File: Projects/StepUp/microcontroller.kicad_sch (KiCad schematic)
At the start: 31 parts, among them J1 USB_C_Receptacle_USB2.0_16P, J2 Conn_01x02, J3 Conn_02x03_Counter_Clockwise, SW1 SW_Push, SW2 SW_Push, U1 USBLC6-2SC6, U2 W25Q128JVS, U3 RP2040, Y1 ABM8-272-T3

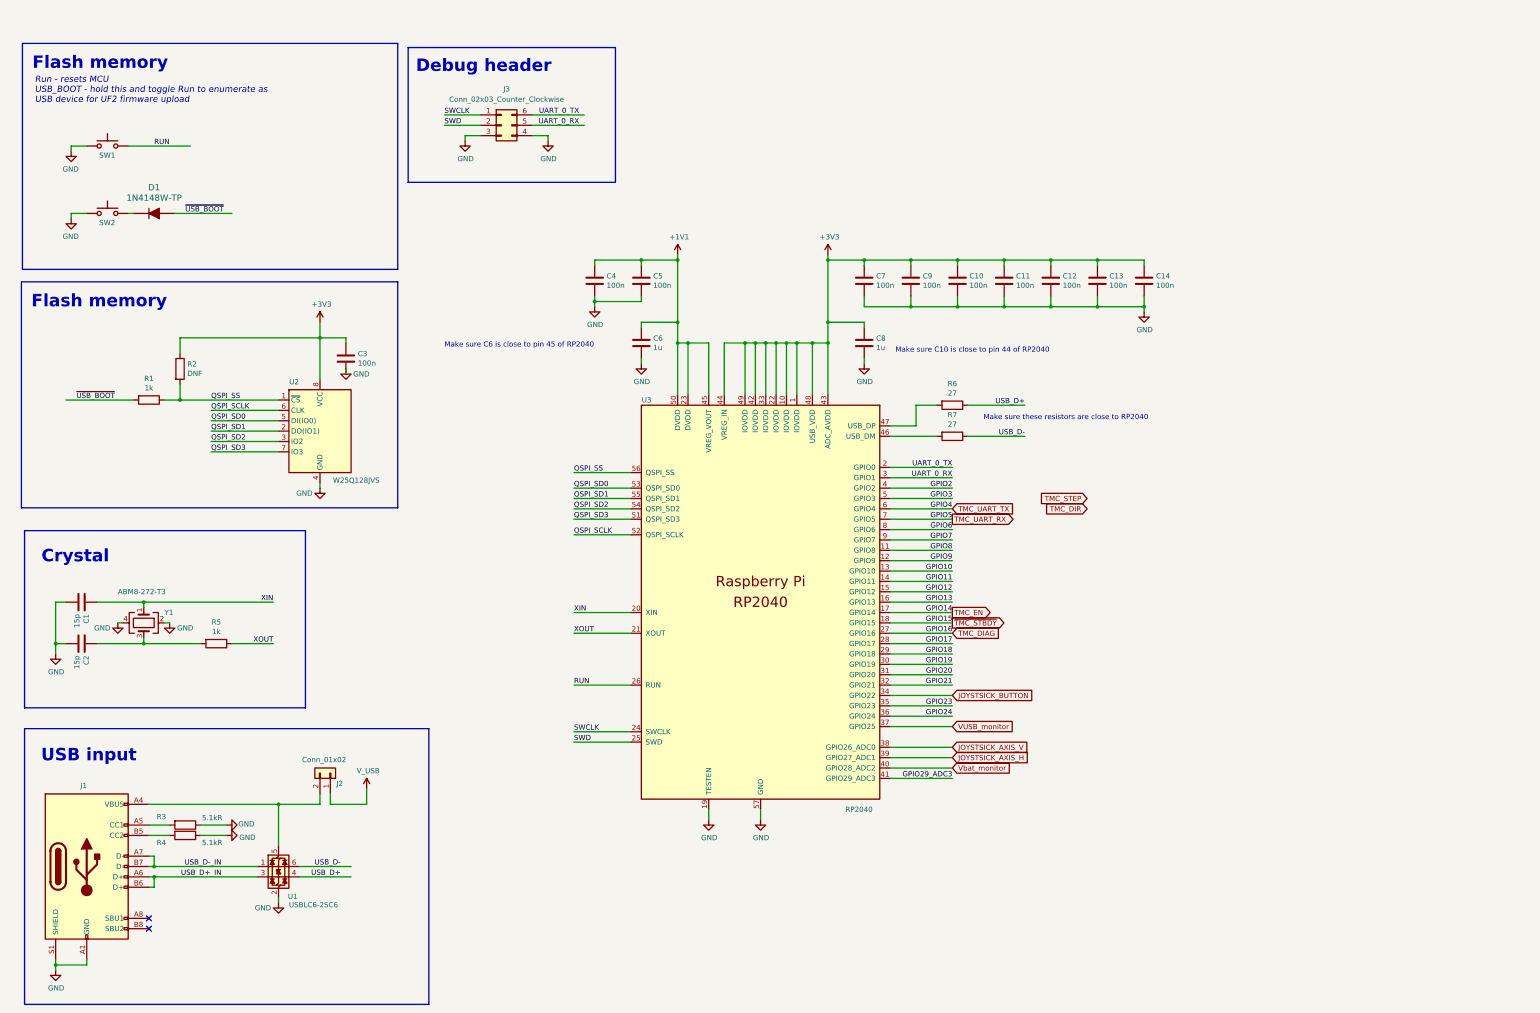
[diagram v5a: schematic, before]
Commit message: feat(schematic): Ready for layout
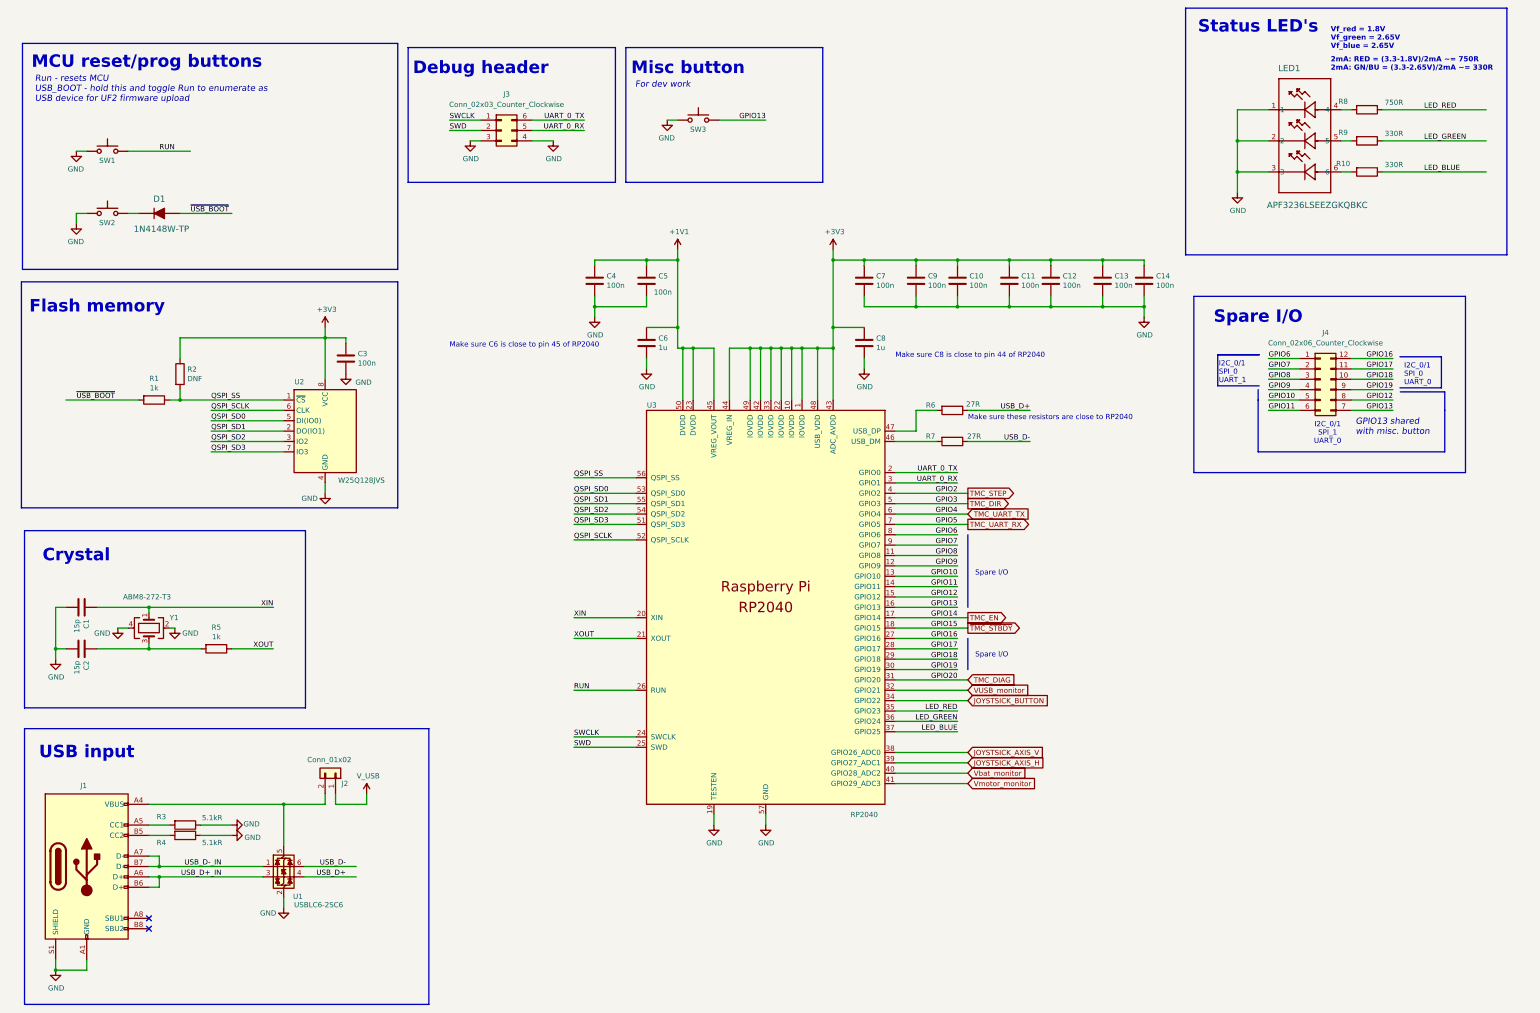
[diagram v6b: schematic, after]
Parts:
- added J4: Conn_02x06_Counter_Clockwise, Connector_PinHeader_2.54mm:PinHeader_2x06_P2.54mm_Vertical, symbol Connector_Generic:Conn_02x06_Counter_Clockwise
- added LED1: APF3236LSEEZGKQBKC, Snapeda:APF3236LSEEZGKQBKC_KNB, symbol Snapeda_kicad_2:APF3236LSEEZGKQBKC
- added R10, R9: 330R, Resistor_SMD:R_0603_1608Metric, symbol Device:R
- added R8: 750R, Resistor_SMD:R_0603_1608Metric, symbol Device:R
- added SW3: SW_Push, Button_Switch_SMD:SW_Push_1P1T_NO_Vertical_Wuerth_434133025816, symbol Switch:SW_Push
- R6, R7: value 27 -> 27R
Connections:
- net GPIO2 is gone; now on net TMC_STEP: U3.4 (GPIO2)
- net GPIO20 is gone; now on net TMC_DIAG: U3.31 (GPIO20)
- net GPIO21 is gone; now on net VUSB_monitor: U3.32 (GPIO21)
- net GPIO3 is gone; now on net TMC_DIR: U3.5 (GPIO3)
- net GND: now also LED1.1, LED1.2, LED1.3, SW3.1
- net GPIO10: now also J4.5 (Pin_5)
- net GPIO11: now also J4.6 (Pin_6)
- net GPIO12: now also J4.8 (Pin_8)
- net GPIO13: now also J4.7 (Pin_7), SW3.2
- net GPIO17: now also J4.11 (Pin_11)
- net GPIO18: now also J4.10 (Pin_10)
- net GPIO19: now also J4.9 (Pin_9)
- net GPIO6: now also J4.1 (Pin_1)
- net GPIO7: now also J4.2 (Pin_2)
- net GPIO8: now also J4.3 (Pin_3)
- net GPIO9: now also J4.4 (Pin_4)
- net TMC_DIAG: no longer U3.27 (GPIO16)
- net VUSB_monitor: no longer U3.37 (GPIO25)
- net GPIO23 renamed LED_RED
- net LED_RED: now also R8.1
- net GPIO24 renamed LED_GREEN
- net LED_GREEN: now also R9.1
- net GPIO29_ADC3 renamed Vmotor_monitor
- new net: LED1.4, R8.2
- new net: LED1.5, R9.2
- new net: LED1.6, R10.2
- new net GPIO16: J4.12 (Pin_12), U3.27 (GPIO16)
- new net LED_BLUE: R10.1, U3.37 (GPIO25)
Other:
- note added: "2mA: RED = (3.3-1.8V)/2mA ~= 750R 2mA: GN/BU = (3.3-2.65V)/2mA ~= 330R"
- note added: "For dev work"
- note added: "GPIO13 shared with misc. button"
- note added: "I2C_0/1 SPI_0 UART_0"
- note added: "I2C_0/1 SPI_0 UART_1"
- note added: "I2C_0/1 SPI_1 UART_0"
- note added: "MCU reset/prog buttons"
- note added: "Make sure C8 is close to pin 44 of RP2040"
- note added: "Misc button"
- note added: "Spare I/O"
- note added: "Status LED's"
- note added: "Vf_red = 1.8V Vf_green = 2.65V Vf_blue = 2.65V"
- note removed: "Make sure C10 is close to pin 44 of RP2040"
- moved on the sheet: C1, C11, C13, C2, C5, C6, C9, D1, J2, J3, R1, R2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

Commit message: chore(pins): MCU_BOOST_EN to MCU, fixed errors
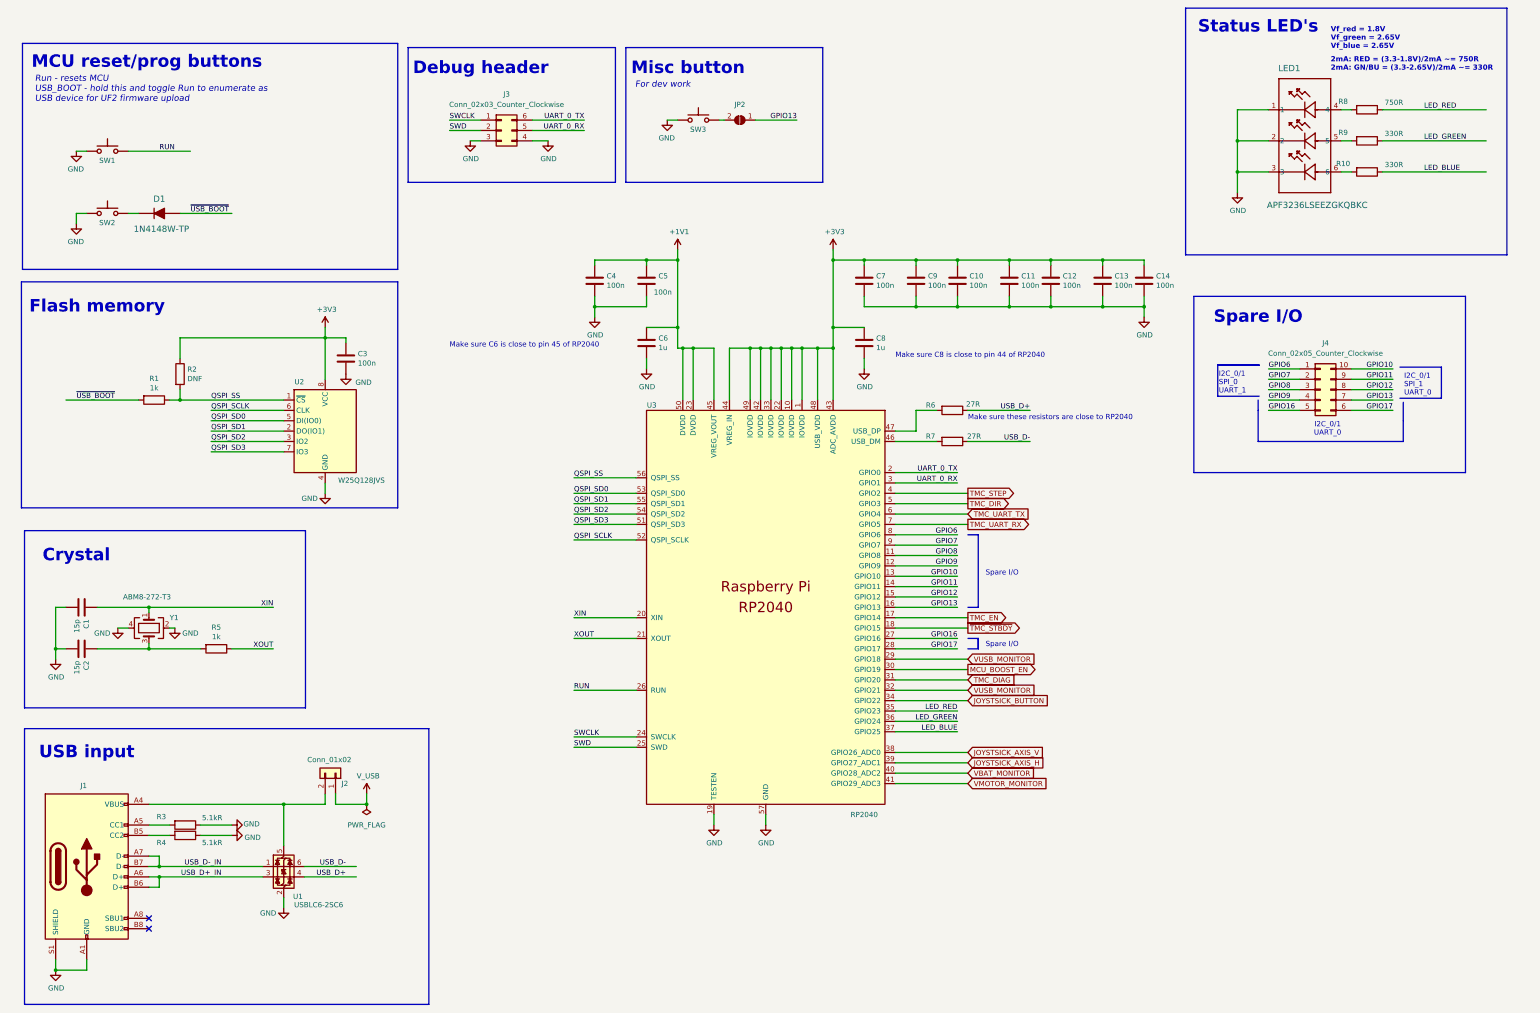
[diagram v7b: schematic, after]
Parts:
- removed J4: Conn_02x06_Counter_Clockwise, Connector_PinHeader_2.54mm:PinHeader_2x06_P2.54mm_Vertical, symbol Connector_Generic:Conn_02x06_Counter_Clockwise
- added J4: Conn_02x05_Counter_Clockwise, Connector_PinHeader_2.54mm:PinHeader_2x05_P2.54mm_Vertical, symbol Connector_Generic:Conn_02x05_Counter_Clockwise
- added JP2: SolderJumper_2_Open, Jumper:SolderJumper-2_P1.3mm_Open_RoundedPad1.0x1.5mm, symbol Jumper:SolderJumper_2_Open
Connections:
- net VUSB_monitor is gone; now on net VUSB_MONITOR: U3.32 (GPIO21)
- net GPIO10: now also J4.10 (Pin_10)
- net GPIO11: now also J4.9 (Pin_9)
- net GPIO12: now also J4.8 (Pin_8)
- net GPIO13: now also J4.7 (Pin_7), JP2.1 (A); no longer SW3.2
- net GPIO16: now also J4.5 (Pin_5)
- net GPIO17: now also J4.6 (Pin_6)
- net GPIO6: now also J4.1 (Pin_1)
- net GPIO7: now also J4.2 (Pin_2)
- net GPIO8: now also J4.3 (Pin_3)
- net GPIO9: now also J4.4 (Pin_4)
- net GPIO18 renamed VUSB_MONITOR
- net GPIO19 renamed MCU_BOOST_EN
- net Vbat_monitor renamed VBAT_MONITOR
- net Vmotor_monitor renamed VMOTOR_MONITOR
- new net: JP2.2 (B), SW3.2
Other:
- note added: "I2C_0/1 UART_0"
- note removed: "GPIO13 shared with misc. button"
- note removed: "I2C_0/1 SPI_0 UART_0"

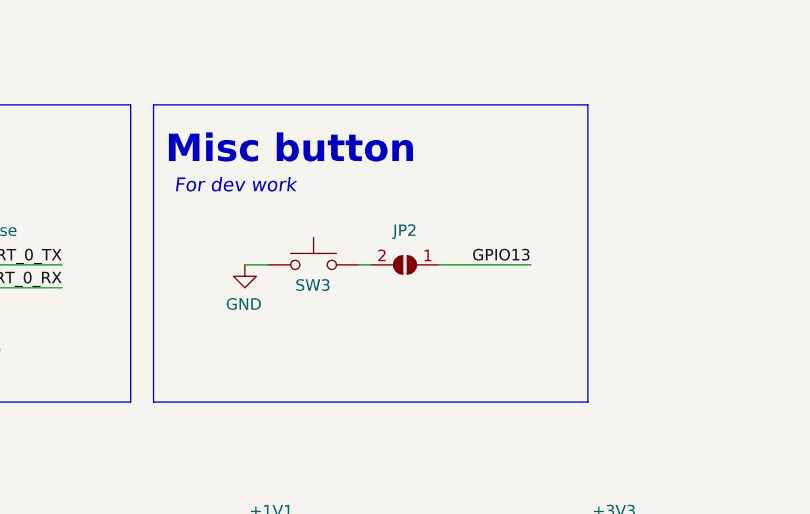
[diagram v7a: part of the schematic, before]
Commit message: feat(layout): Blocks organised
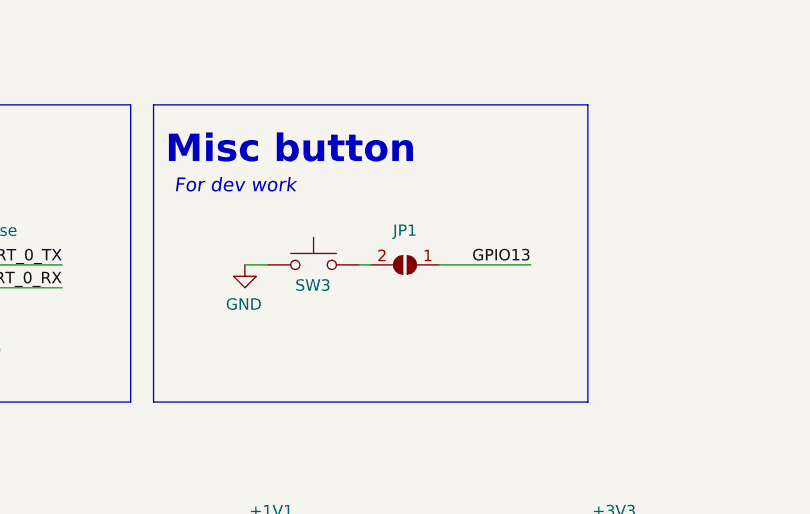
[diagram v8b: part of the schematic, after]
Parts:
- renumbered JP2 to JP1
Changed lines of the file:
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@@
 		(dnp no)
 		(fields_autoplaced yes)
-		(property "Reference" "JP2"
+		(property "Reference" "JP1"
 			(at 208.28 41.91 0)
 			(effects
@@
 			(project "StepUp"
 				(path "/e0cca1c7-c263-49eb-8c40-74000ebe5285/3af138f5-65b6-4464-96c0-d1b764f3b0d1"
-					(reference "JP2")
+					(reference "JP1")
 					(unit 1)
 				)
@@
 		(dnp no)
 		(fields_autoplaced yes)
-		(property "Reference" "#FLG05"
+		(property "Reference" "#FLG01"
 			(at 116.84 215.265 0)
 			(effects
@@
 			(project "StepUp"
 				(path "/e0cca1c7-c263-49eb-8c40-74000ebe5285/3af138f5-65b6-4464-96c0-d1b764f3b0d1"
-					(reference "#FLG05")
+					(reference "#FLG01")
 					(unit 1)
 				)
@@
 			(effects
 				(font
-					(size 1.524 1.524)
-				)
-				(justify left)
-				(hide yes)
-			)
-		)
-		(property "Description" "DIODE GEN PURP 100V 150MA SOD123"
-			(at 60.96 93.98 0)
-			(effects
-				(font
